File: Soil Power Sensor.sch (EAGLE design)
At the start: 77 parts, among them J1 12401832E402A, U10 TPS7A20330PDBVR, U11 TPS60403DBVR, U12 REF1933AIDDCR, U13 TLV1117LV33DCYR, U14 FSA2466UMX, U2 FT234XD-R, U3 MAX9944ATA+T, U4 ESP32-C3-MINI-1-N4, U5 LTC6362CDDPBF, U6 LTC6362CDDPBF, U7 INA296A5, U8 MAX11201AEUB+, U9 MAX11201AEUB+, X1 SMA-142-0701-801/806

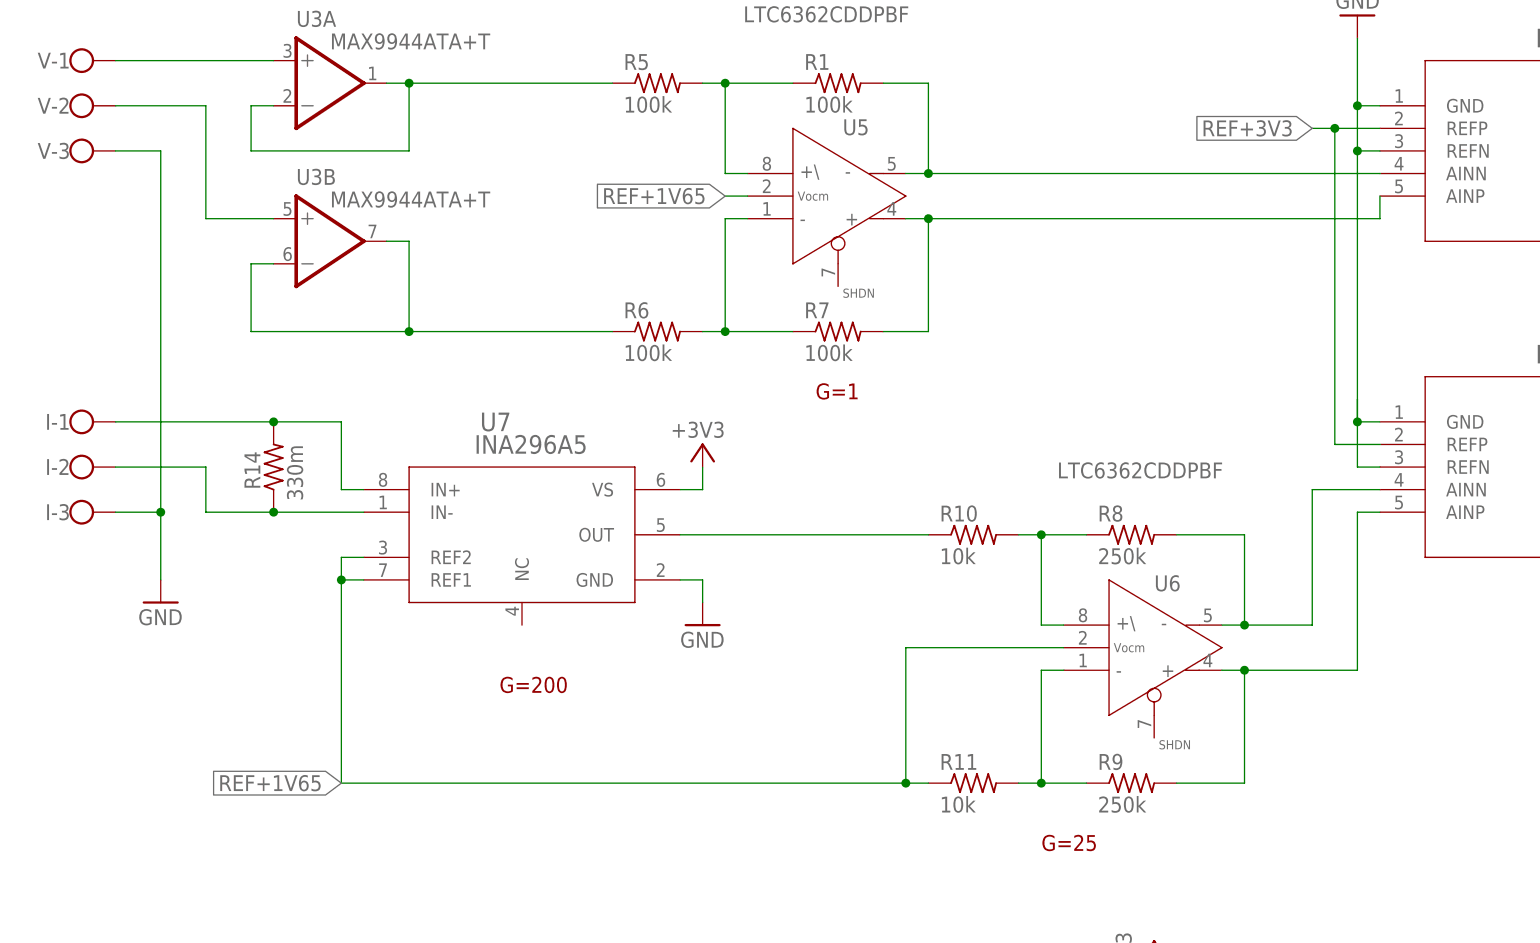
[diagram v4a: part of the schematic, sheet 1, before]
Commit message: Added LP filter on signals leading to ADC
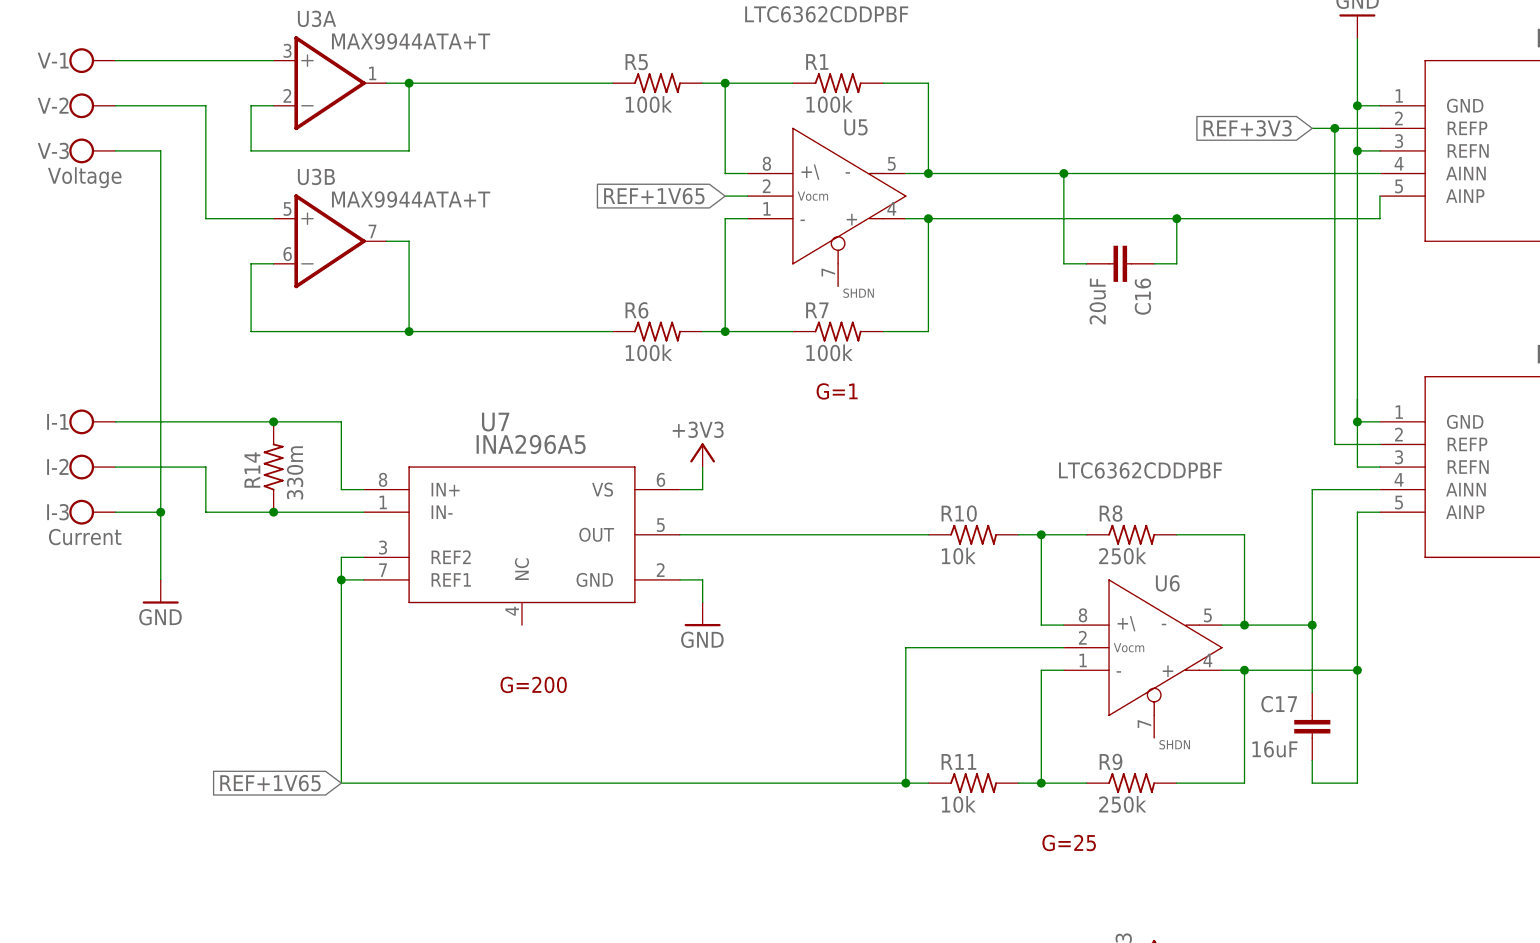
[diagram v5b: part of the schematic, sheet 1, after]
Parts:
- added C16: 20uF, rcl:C-EUC0603
- added C17: 16uF, rcl:C-EUC0603
- I: value (none) -> Current
- V: value (none) -> Voltage
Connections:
- net N$31: now also C16.2
- net N$32: now also C16.1
- net N$34: now also C17.2
- net N$35: now also C17.1
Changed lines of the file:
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@@
 <part name="C31" library="rcl" library_urn="urn:adsk.eagle:library:334" deviceset="C-EU" device="C0402" package3d_urn="urn:adsk.eagle:package:23626/2" value="0.1uF"/>
 <part name="GND25" library="supply1" library_urn="urn:adsk.eagle:library:371" deviceset="GND" device=""/>
-<part name="V" library="con-wago-500" library_urn="urn:adsk.eagle:library:195" deviceset="W237-103" device="" package3d_urn="urn:adsk.eagle:package:10691/1"/>
+<part name="V" library="con-wago-500" library_urn="urn:adsk.eagle:library:195" deviceset="W237-103" device="" package3d_urn="urn:adsk.eagle:package:10691/1" value="Voltage"/>
 <part name="GND26" library="supply1" library_urn="urn:adsk.eagle:library:371" deviceset="GND" device=""/>
 <part name="R1" library="rcl" library_urn="urn:adsk.eagle:library:334" deviceset="R-US_" device="R0402" package3d_urn="urn:adsk.eagle:package:23547/3" value="100k"/>
@@
 <part name="GND9" library="supply1" library_urn="urn:adsk.eagle:library:371" deviceset="GND" device=""/>
 <part name="+3V2" library="supply1" library_urn="urn:adsk.eagle:library:371" deviceset="+3V3" device=""/>
-<part name="I" library="con-wago-500" library_urn="urn:adsk.eagle:library:195" deviceset="W237-103" device="" package3d_urn="urn:adsk.eagle:package:10691/1"/>
+<part name="I" library="con-wago-500" library_urn="urn:adsk.eagle:library:195" deviceset="W237-103" device="" package3d_urn="urn:adsk.eagle:package:10691/1" value="Current"/>
+<part name="C16" library="rcl" library_urn="urn:adsk.eagle:library:334" deviceset="C-EU" device="C0603" package3d_urn="urn:adsk.eagle:package:23616/2" value="20uF"/>
+<part name="C17" library="rcl" library_urn="urn:adsk.eagle:library:334" deviceset="C-EU" device="C0603" package3d_urn="urn:adsk.eagle:package:23616/2" value="16uF"/>
 </parts>
 <sheets>
@@
 <attribute name="VALUE" x="12.7" y="100.457" size="1.778" layer="96"/>
 <attribute name="NAME" x="15.24" y="105.029" size="1.778" layer="95" rot="R180"/>
+</instance>
+<instance part="C16" gate="G$1" x="134.62" y="132.08" smashed="yes" rot="R270">
+<attribute name="NAME" x="135.001" y="130.556" size="1.778" layer="95" rot="R270"/>
+<attribute name="VALUE" x="129.921" y="130.556" size="1.778" layer="96" rot="R270"/>
+</instance>
+<instance part="C17" gate="G$1" x="154.94" y="81.28" smashed="yes" rot="MR0">
+<attribute name="NAME" x="153.416" y="81.661" size="1.778" layer="95" rot="MR0"/>
+<attribute name="VALUE" x="153.416" y="76.581" size="1.778" layer="96" rot="MR0"/>
 </instance>
 </instances>
@@
 <wire x1="109.22" y1="142.24" x2="111.76" y2="142.24" width="0.1524" layer="91"/>
 <pinref part="R1" gate="G$1" pin="2"/>
-<wire x1="111.76" y1="142.24" x2="162.56" y2="142.24" width="0.1524" layer="91"/>
+<wire x1="111.76" y1="142.24" x2="127" y2="142.24" width="0.1524" layer="91"/>
+<wire x1="127" y1="142.24" x2="162.56" y2="142.24" width="0.1524" layer="91"/>
 <wire x1="106.68" y1="152.4" x2="111.76" y2="152.4" width="0.1524" layer="91"/>
 <wire x1="111.76" y1="152.4" x2="111.76" y2="142.24" width="0.1524" layer="91"/>
 <junction x="111.76" y="142.24"/>
+<pinref part="C16" gate="G$1" pin="2"/>
+<wire x1="129.54" y1="132.08" x2="127" y2="132.08" width="0.1524" layer="91"/>
+<wire x1="127" y1="132.08" x2="127" y2="142.24" width="0.1524" layer="91"/>
+<junction x="127" y="142.24"/>
 </segment>
 </net>
@@
 <pinref part="U8" gate="A" pin="AINP"/>
 <wire x1="109.22" y1="137.16" x2="111.76" y2="137.16" width="0.1524" layer="91"/>
-<wire x1="111.76" y1="137.16" x2="162.56" y2="137.16" width="0.1524" layer="91"/>
+<wire x1="111.76" y1="137.16" x2="139.7" y2="137.16" width="0.1524" layer="91"/>
+<wire x1="139.7" y1="137.16" x2="162.56" y2="137.16" width="0.1524" layer="91"/>
 <wire x1="162.56" y1="137.16" x2="162.56" y2="139.7" width="0.1524" layer="91"/>
 <pinref part="R7" gate="G$1" pin="2"/>
@@
 <wire x1="111.76" y1="124.46" x2="111.76" y2="137.16" width="0.1524" layer="91"/>
 <junction x="111.76" y="137.16"/>
+<pinref part="C16" gate="G$1" pin="1"/>
+<wire x1="137.16" y1="132.08" x2="139.7" y2="132.08" width="0.1524" layer="91"/>
+<wire x1="139.7" y1="132.08" x2="139.7" y2="137.16" width="0.1524" layer="91"/>
+<junction x="139.7" y="137.16"/>
 </segment>
 </net>
@@
 <pinref part="U9" gate="A" pin="AINP"/>
 <wire x1="160.02" y1="104.14" x2="162.56" y2="104.14" width="0.1524" layer="91"/>
+<pinref part="C17" gate="G$1" pin="2"/>
+<wire x1="154.94" y1="76.2" x2="154.94" y2="73.66" width="0.1524" layer="91"/>
+<wire x1="154.94" y1="73.66" x2="160.02" y2="73.66" width="0.1524" layer="91"/>
+<wire x1="160.02" y1="73.66" x2="160.02" y2="86.36" width="0.1524" layer="91"/>
+<junction x="160.02" y="86.36"/>
 </segment>
 </net>
@@
 <pinref part="U9" gate="A" pin="AINN"/>
 <wire x1="154.94" y1="106.68" x2="162.56" y2="106.68" width="0.1524" layer="91"/>
-</segment>
-</net>
+<pinref part="C17" gate="G$1" pin="1"/>
+<wire x1="154.94" y1="83.82" x2="154.94" y2="91.44" width="0.1524" layer="91"/>
+<junction x="154.94" y="91.44"/>
+</segment>
+</net>

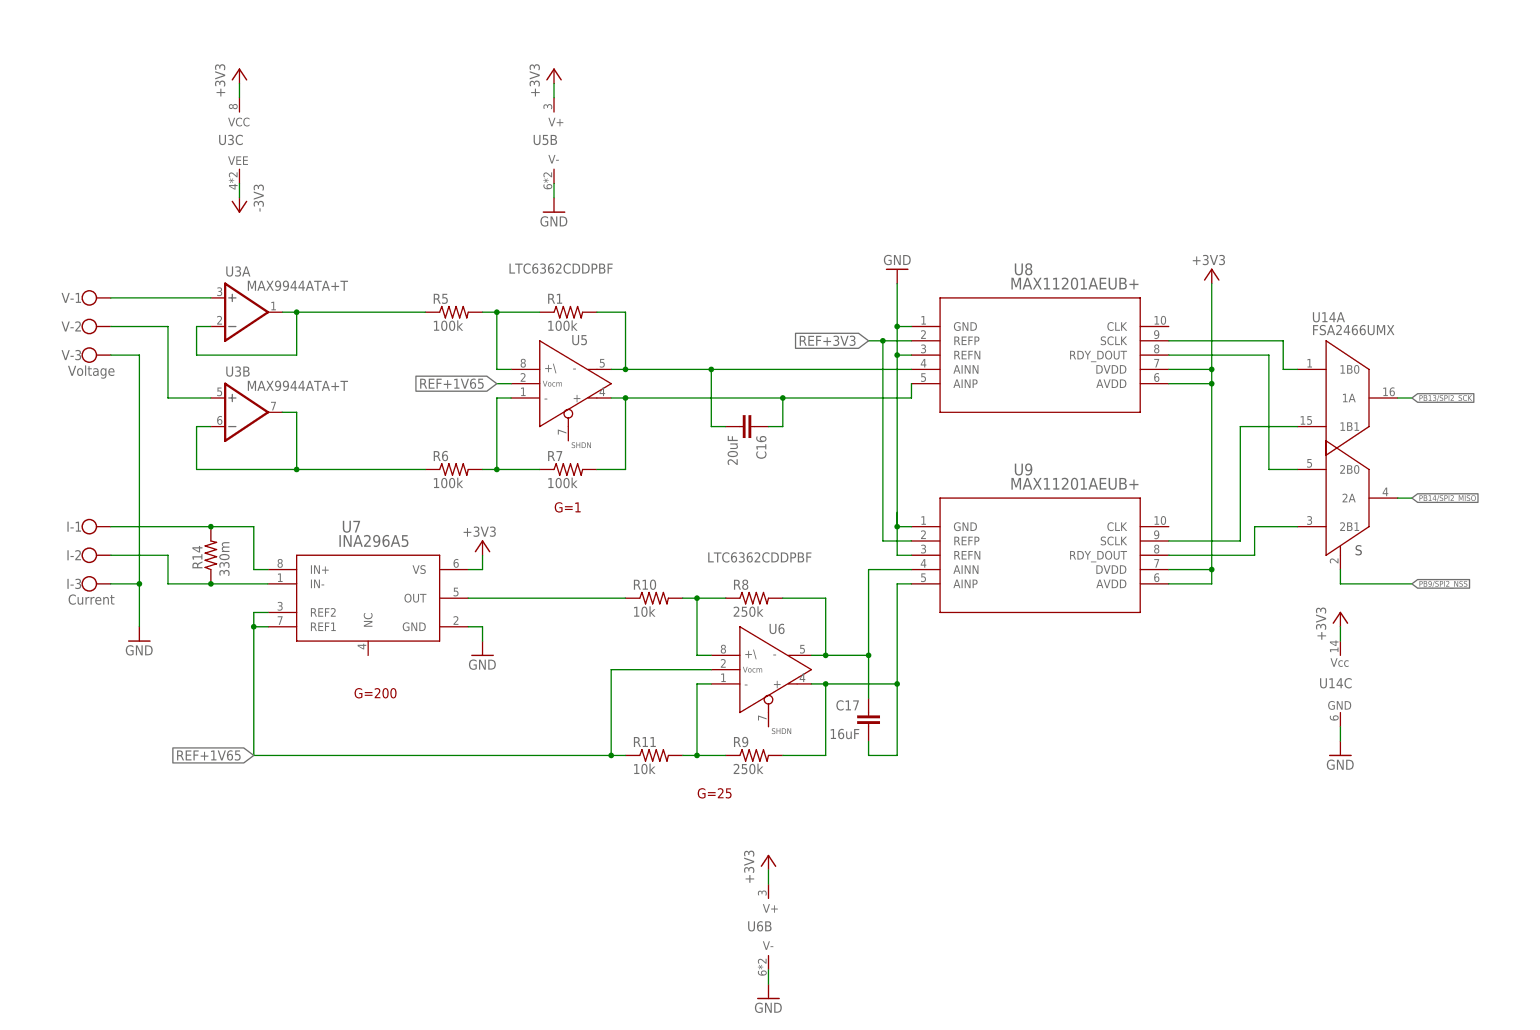
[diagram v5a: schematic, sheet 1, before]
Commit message: Added test points
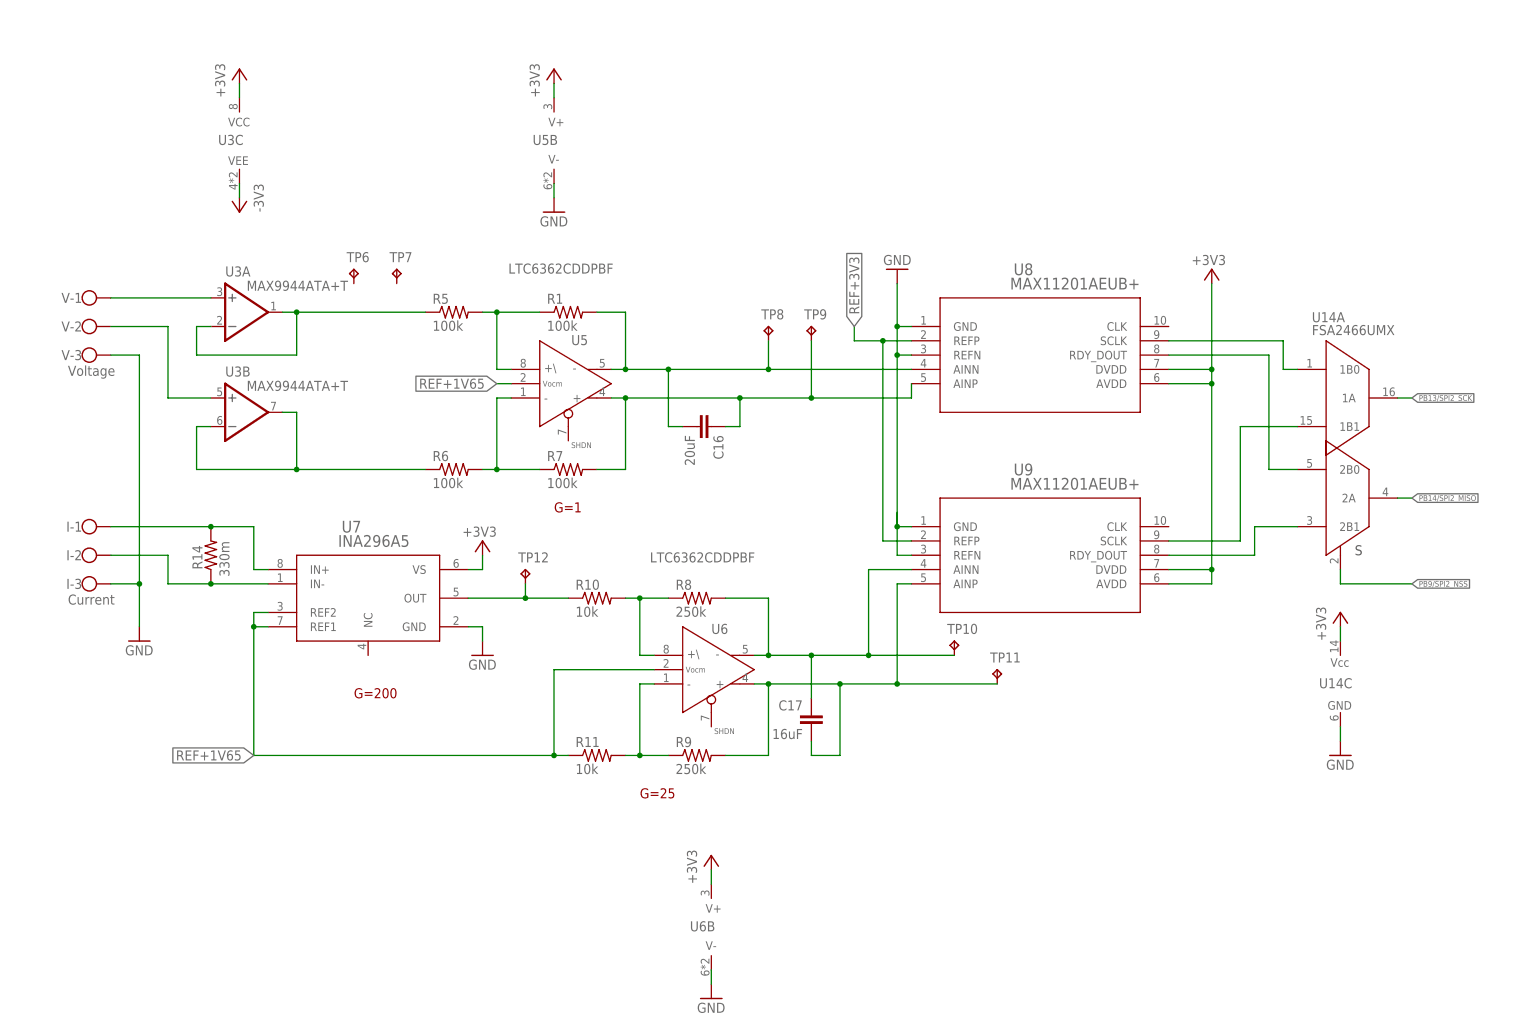
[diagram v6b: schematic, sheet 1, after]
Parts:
- added TP1, TP10, TP11, TP12, TP2, TP3, TP4, TP5, TP6, TP7, TP8, TP9: TPB1,27, testpad:TPB1,27
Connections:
- removed net N$34: C17.2, R9.2, U6A.OUT+, U9.AINP
- new net N$47: C17.2, R9.2, TP11.TP, U6A.OUT+, U9.AINP
- net +3V3: now also TP2.TP
- net -3V3: now also TP1.TP
- net N$31: now also TP8.TP
- net N$32: now also TP9.TP
- net N$35: now also TP10.TP
- net N$37: now also TP12.TP
- net REF+1V65: now also TP4.TP
- net REF+3V3: now also TP3.TP
- net VCC: now also TP5.TP
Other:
- moved on the sheet: C16, C17, R10, R11, R8, R9, U6, U6B
